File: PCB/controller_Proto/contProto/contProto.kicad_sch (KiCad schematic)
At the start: 83 parts, among them J1 Conn_01x05, J10 JST_1mm_3, J11 JST_1mm_3, J12 JST_1mm_3, J13 Conn_01x02_Socket, J14 Conn_01x02_Socket, J15 Conn_01x04, J16 Conn_01x04, J17 Conn_01x10_Pin, J18 JST_1mm_3, J19 Conn_01x08_Socket, J2 Conn_01x04, J20 JST_1mm_3, J21 JST_1mm_3, J22 JST_1mm_3, J23 JST_1mm_3, J24 Conn_01x03_Socket, J25 Conn_01x03_Socket, J26 Conn_01x03_Socket, J27 Conn_01x03_Socket, J28 Conn_01x12_Socket, J29 Conn_01x12_Socket, J3 Conn_01x10_Pin, J30 Conn_01x12_Socket, J31 Conn_01x12_Socket, J32 Conn_01x02_Socket, J33 Conn_01x02_Socket, J34 Conn_01x02_Socket, J35 Conn_01x02_Socket, J4 JST_1mm_3, J5 Conn_01x05, J6 JST_1mm_3, J7 Conn_01x05, J8 Conn_01x05, J9 Conn_01x04, SW1 SMD_12x12mm_h8.5mm, SW10 SMD_12x12mm_h8.5mm, SW11 SMD_12x12mm_h8.5mm, SW12 SMD_12x12mm_h8.5mm, SW13 SMD_12x12mm_h8.5mm, SW14 SMD_12x12mm_h8.5mm, SW15 SMD_12x12mm_h8.5mm, SW16 SMD_12x12mm_h8.5mm, SW17 SMD_12x12mm_h8.5mm, SW18 SMD_12x12mm_h8.5mm, SW19 SMD_12x12mm_h8.5mm, SW2 SMD_12x12mm_h8.5mm, SW20 SMD_12x12mm_h8.5mm, SW3 SMD_12x12mm_h8.5mm, SW4 SMD_12x12mm_h8.5mm, SW5 SMD_12x12mm_h8.5mm, SW6 SMD_12x12mm_h8.5mm, SW7 SMD_12x12mm_h8.5mm, SW8 SMD_12x12mm_h8.5mm, SW9 SMD_12x12mm_h8.5mm, U1 ProMicroC, U2 ProMicroC, U3 DRV5033FAxLPG, U4 DRV5033FAxLPG

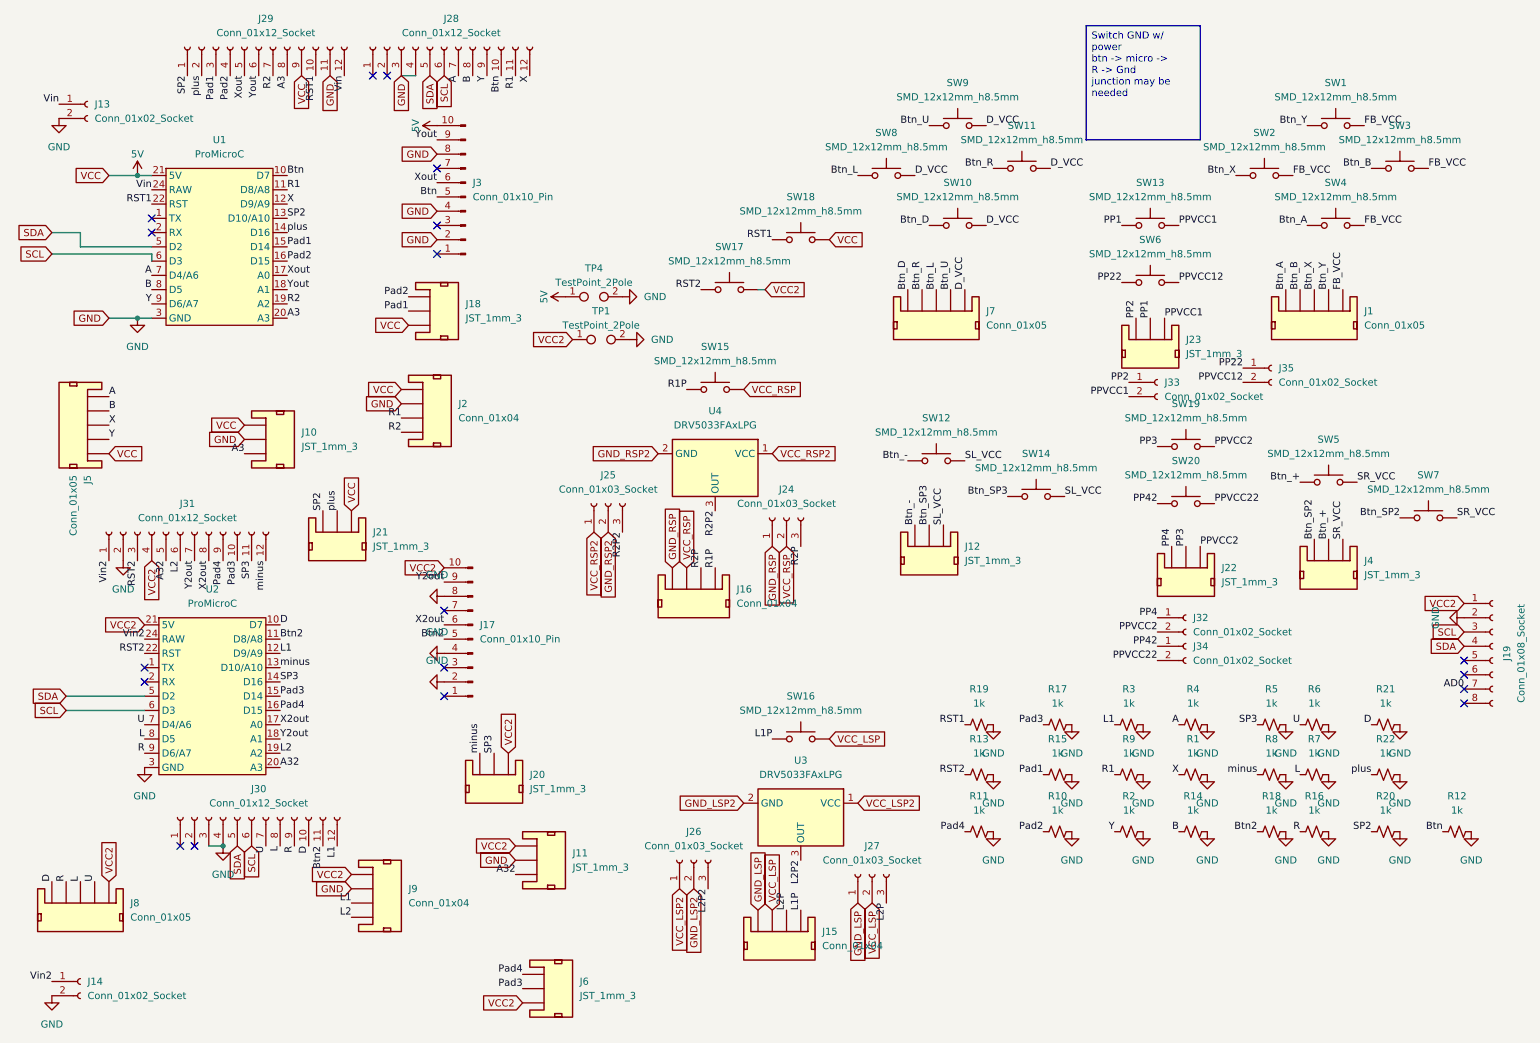
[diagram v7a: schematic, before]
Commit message: no more errors and trackball ports
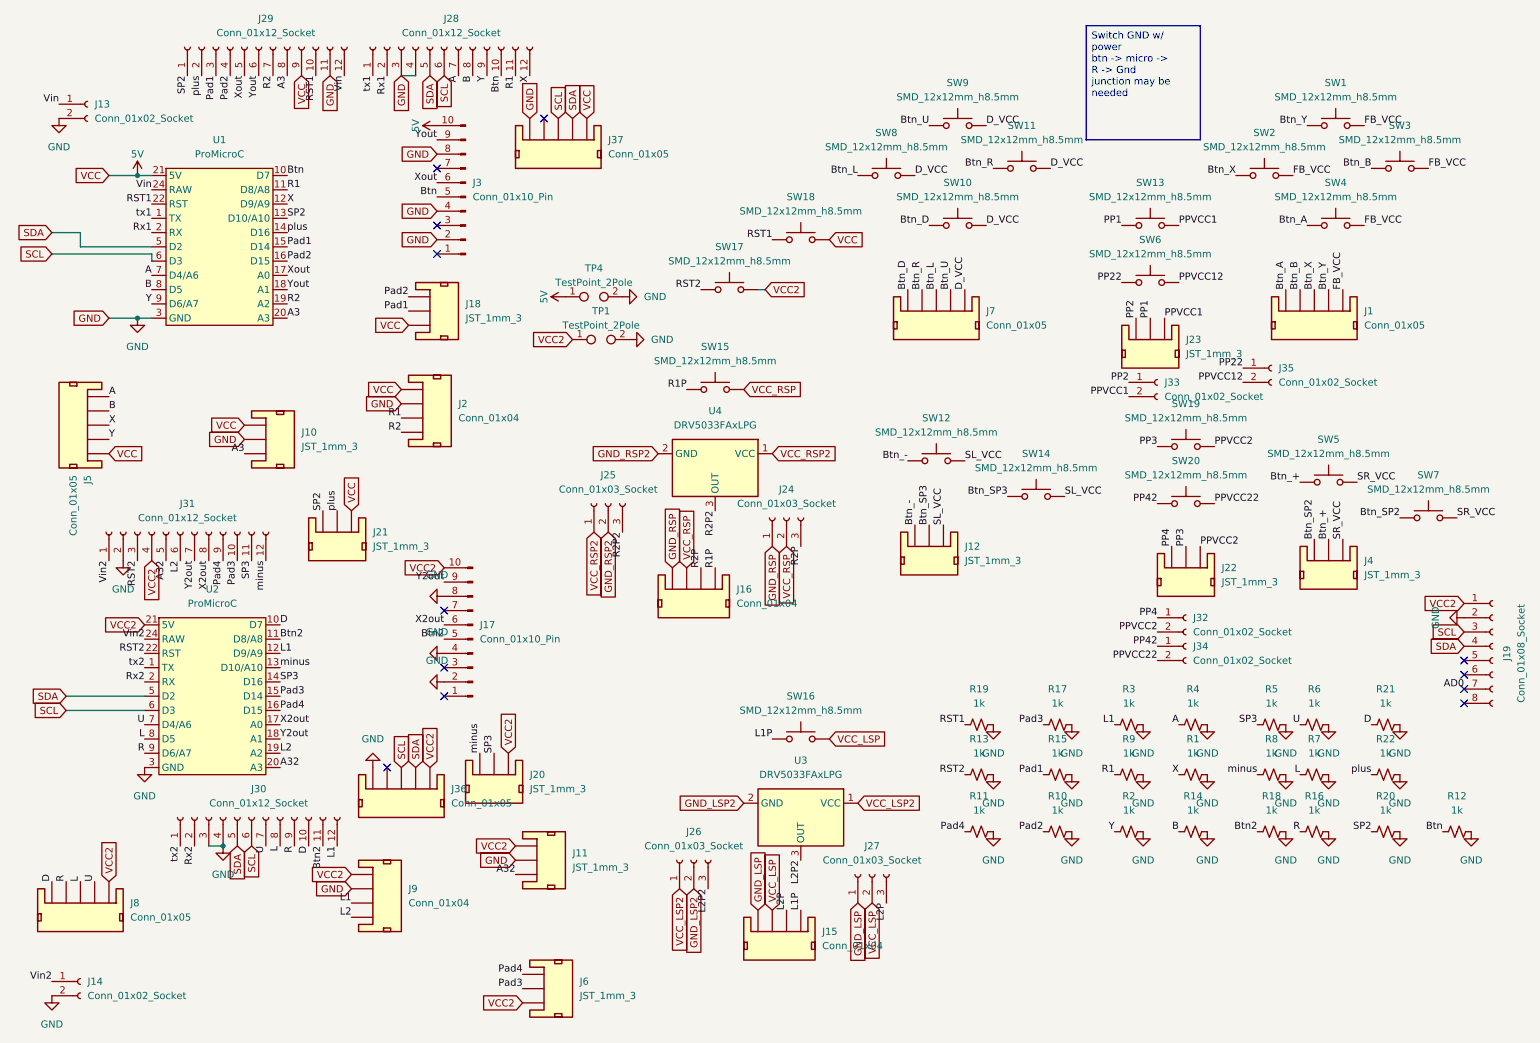
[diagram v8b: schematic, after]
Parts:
- added J36, J37: Conn_01x05, Connector_JST:JST_GH_BM05B-GHS-TBT_1x05-1MP_P1.25mm_Vertical, symbol PCM_SparkFun-Connector:Conn_01x05_JST_P1.0mm_Horizontal_SMD
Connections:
- net 5V: now also J37.1
- net GND: now also J36.5, J37.5
- net SCL: now also J36.3, J37.3
- net SDA: now also J36.2, J37.2
- net VCC2: now also J36.1
- net tx1: now reaches J28.1 (Pin_1)
- net tx1: now also U1.1 (TX)
- net Rx1: now reaches J28.2 (Pin_2)
- net Rx1: now also U1.2 (RX)
- net tx2: now reaches J30.1 (Pin_1)
- net tx2: now also U2.1 (TX)
- net Rx2: now reaches J30.2 (Pin_2)
- net Rx2: now also U2.2 (RX)
- no-connect marks 18 -> 12
